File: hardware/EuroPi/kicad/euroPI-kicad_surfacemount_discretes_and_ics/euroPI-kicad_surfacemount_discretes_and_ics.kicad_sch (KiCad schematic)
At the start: 119 parts, among them J1 Output 1 Jack, J10 Eurorack Power 2x8 16p, J11 Conn_01x13_Socket, J12 OLED 64x128, J13 USB_B_Micro, J14 Conn_01x03_Pin, J15 Conn_01x04_Pin, J16 Conn_02x04_Top_Bottom, J17 Conn_01x13_Pin, J18 Conn_01x04_Pin, J19 Conn_01x04_Socket, J2 Output 2 Jack, J21 Conn_01x03_Pin, J3 Output 3 Jack, J4 Output 4 Jack, J5 Output 5 Jack, J6 Output 6 Jack, J7 Digital Input Jack, J8 Analogue Input Jack, Q1 2N2222, SW1 SW_Push, SW2 SW_Push, U3 LM555xN

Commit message: euroPI kicad version now including SMDs
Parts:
- C1, C10, C11, C12, C13, C14, C15, C16, C2, C3, C4, C5, C6, C7, C8, C9: footprint Capacitor_THT:C_Radial_D5.0mm_H11.0mm_P2.00mm -> Capacitor_SMD:C_0805_2012Metric_Pad1.18x1.45mm_HandSolder
- D1, D2, D3, D4: footprint Diode_THT:D_A-405_P2.54mm_Vertical_KathodeUp -> Diode_SMD:D_0805_2012Metric_Pad1.15x1.40mm_HandSolder
- O, O? (x8): footprint Package_DIP:DIP-14_W7.62mm_Socket -> Package_SO:SO-14_3.9x8.65mm_P1.27mm
- O1, O? (x2), U3: footprint Package_DIP:DIP-8_W7.62mm -> Package_SO:SO-8_3.9x4.9mm_P1.27mm
- Q1: footprint Package_TO_SOT_THT:TO-92 -> Package_TO_SOT_SMD:SOT-23
- R1, R10, R11, R12, R13, R14, R15, R16, R17, R18, R19, R2, R20, R21, R22, R23, R24, R25, R26, R27, R28, R29, R3, R30, R31, R32, R33, R34, R35, R36, R37, R38, R39, R4, R40, R5, R6, R7, R8, R9: footprint Resistor_THT:R_Axial_DIN0207_L6.3mm_D2.5mm_P5.08mm_Vertical -> Resistor_SMD:R_0805_2012Metric_Pad1.20x1.40mm_HandSolder
- U?: footprint Package_TO_SOT_THT:TO-220-3_Vertical -> Package_TO_SOT_SMD:TO-252-3_TabPin2

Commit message: kicad smd :)
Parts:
- D1, D2, D3, D4: footprint Diode_SMD:D_0805_2012Metric_Pad1.15x1.40mm_HandSolder -> Diode_SMD:D_SOD-123
- Q1: footprint Package_TO_SOT_SMD:SOT-23 -> Package_TO_SOT_THT:TO-92
- U?: footprint Package_TO_SOT_SMD:TO-252-3_TabPin2 -> Package_TO_SOT_THT:TO-220-3_Vertical
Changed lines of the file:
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@@
       (effects (font (size 1.27 1.27)))
     )
-    (property "Footprint" "Diode_SMD:D_0805_2012Metric_Pad1.15x1.40mm_HandSolder" (at 280.67 224.79 0)
+    (property "Footprint" "Diode_SMD:D_SOD-123" (at 280.67 224.79 0)
       (effects (font (size 1.27 1.27)) hide)
     )
@@
       (effects (font (size 1.27 1.27)) (justify left) hide)
     )
-    (property "Sim.Params" "type=\"D\" model=\"DIODE\" lib=\"\"" (at 191.77 5.08 0)
+    (property "Sim.Params" "1N4448W" (at 191.77 5.08 0)
       (effects (font (size 0 0)) hide)
     )
@@
       (effects (font (size 1.27 1.27)))
     )
-    (property "Footprint" "Diode_SMD:D_0805_2012Metric_Pad1.15x1.40mm_HandSolder" (at 364.49 186.69 0)
+    (property "Footprint" "Diode_SMD:D_SOD-123" (at 364.49 186.69 0)
       (effects (font (size 1.27 1.27)) hide)
     )
@@
       (effects (font (size 1.27 1.27)) (justify left) hide)
     )
-    (property "Sim.Params" "type=\"D\" model=\"DIODE\" lib=\"\"" (at 0 0 0)
+    (property "Sim.Params" "1N4448W" (at 0 0 0)
       (effects (font (size 0 0)) hide)
     )
@@
       (effects (font (size 1.27 1.27)) (justify left))
     )
-    (property "Footprint" "Package_TO_SOT_SMD:SOT-23" (at 374.65 177.165 0)
+    (property "Footprint" "Package_TO_SOT_THT:TO-92" (at 374.65 177.165 0)
       (effects (font (size 1.27 1.27) italic) (justify left) hide)
     )
@@
       (effects (font (size 1.27 1.27)))
     )
-    (property "Footprint" "Package_TO_SOT_SMD:TO-252-3_TabPin2" (at 52.705 87.63 0)
+    (property "Footprint" "Package_TO_SOT_THT:TO-220-3_Vertical" (at 52.705 87.63 0)
       (effects (font (size 1.27 1.27) italic) (justify left) hide)
     )
@@
       (effects (font (size 1.27 1.27)) hide)
     )
-    (property "Footprint" "Diode_SMD:D_0805_2012Metric_Pad1.15x1.40mm_HandSolder" (at 73.66 54.61 0)
+    (property "Footprint" "Diode_SMD:D_SOD-123" (at 73.66 54.61 0)
       (effects (font (size 1.27 1.27)) hide)
     )
@@
       (effects (font (size 1.27 1.27)) (justify left) hide)
     )
-    (property "Sim.Params" "type=\"D\" model=\"DIODE\" lib=\"\"" (at 3.81 7.62 0)
+    (property "Sim.Params" "1N4448W" (at 3.81 7.62 0)
       (effects (font (size 0 0)) hide)
     )
@@
       (effects (font (size 1.27 1.27)) hide)
     )
-    (property "Footprint" "Diode_SMD:D_0805_2012Metric_Pad1.15x1.40mm_HandSolder" (at 73.66 44.45 0)
+    (property "Footprint" "Diode_SMD:D_SOD-123" (at 73.66 44.45 0)
       (effects (font (size 1.27 1.27)) hide)
     )
@@
       (effects (font (size 1.27 1.27)) (justify left) hide)
     )
-    (property "Sim.Params" "type=\"D\" model=\"DIODE\" lib=\"\"" (at 3.81 7.62 0)
+    (property "Sim.Params" "1N4448W" (at 3.81 7.62 0)
       (effects (font (size 0 0)) hide)
     )

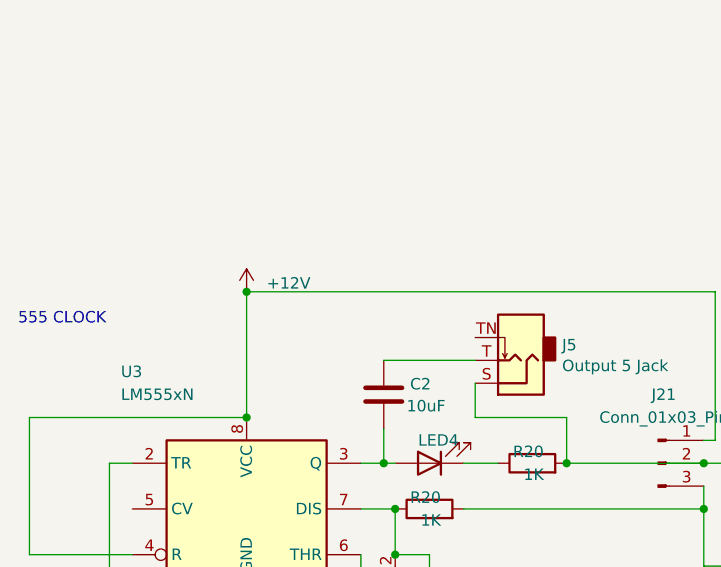
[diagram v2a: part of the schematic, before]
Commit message: misc improvements THT fixed grounds and misc clean up issue likely still wtih usb output SMT redid caps to be near to necessary fixed GND and misc things to make it easier to hand solder
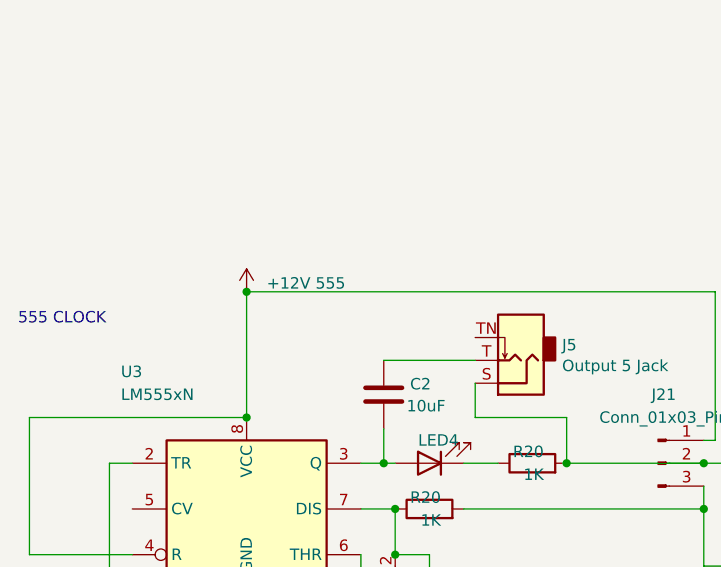
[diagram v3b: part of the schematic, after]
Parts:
- Reference?: value +12V -> +12V 555
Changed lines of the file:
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@@
       (effects (font (size 1.27 1.27)) hide)
     )
-    (property "Value" "+12V" (at -93.0148 85.4202 0)
+    (property "Value" "+12V 555" (at -93.0148 85.4202 0)
       (effects (font (size 1.27 1.27)) (justify left))
     )

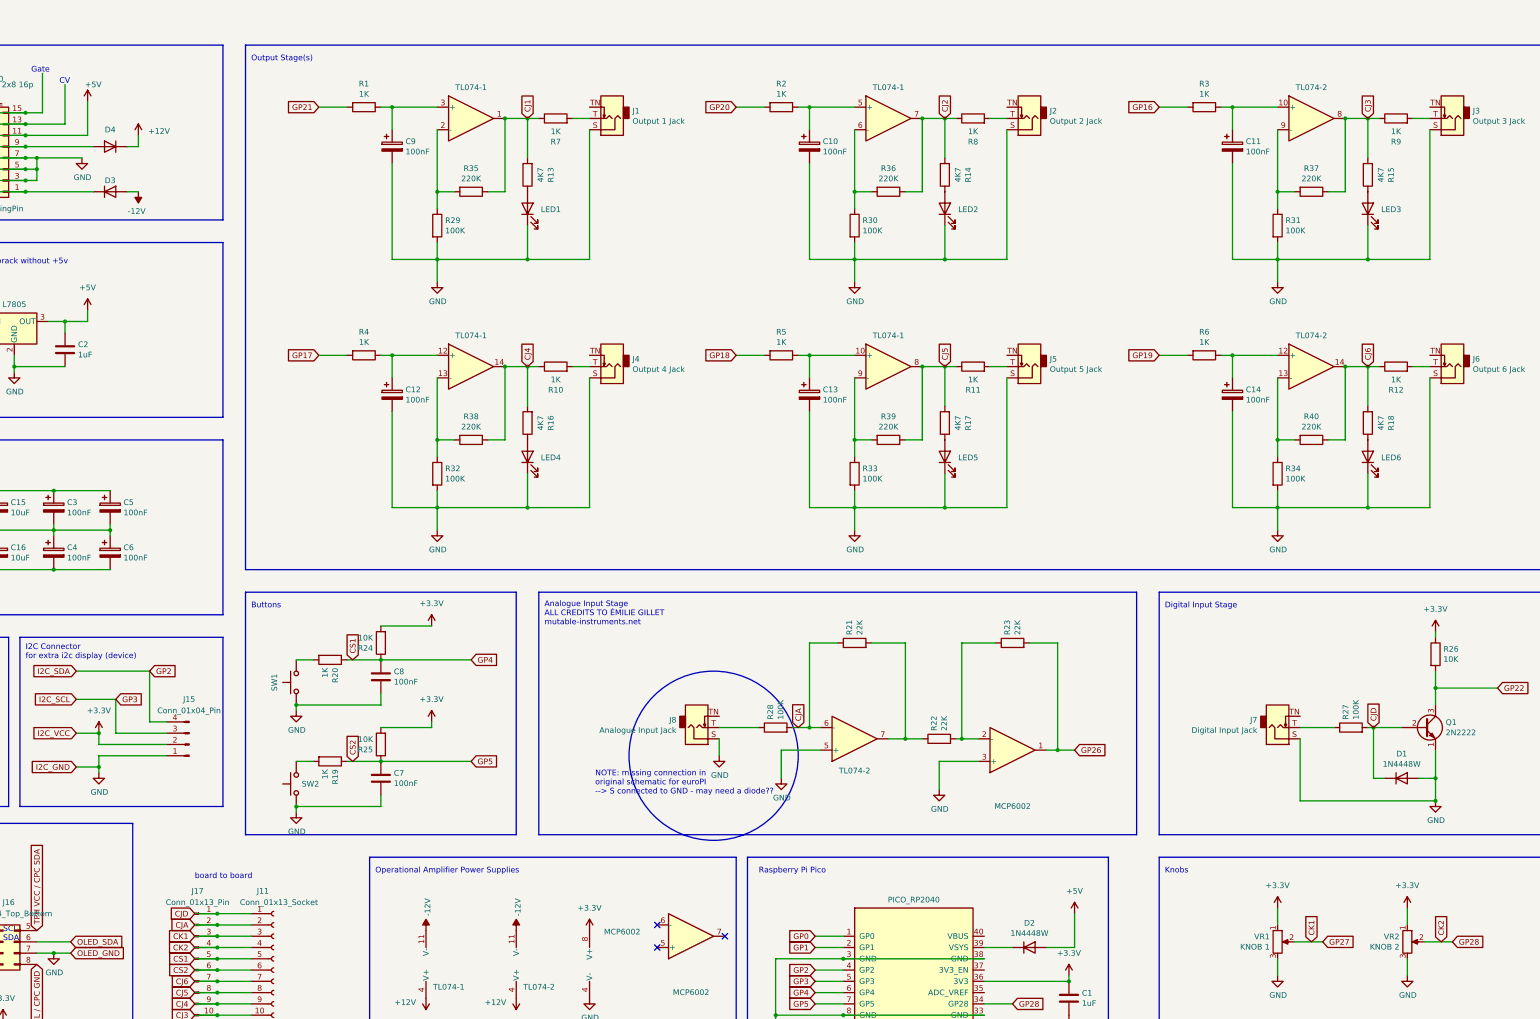
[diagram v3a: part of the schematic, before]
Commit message: some updates of smt version incl correcting layout component choices support structures
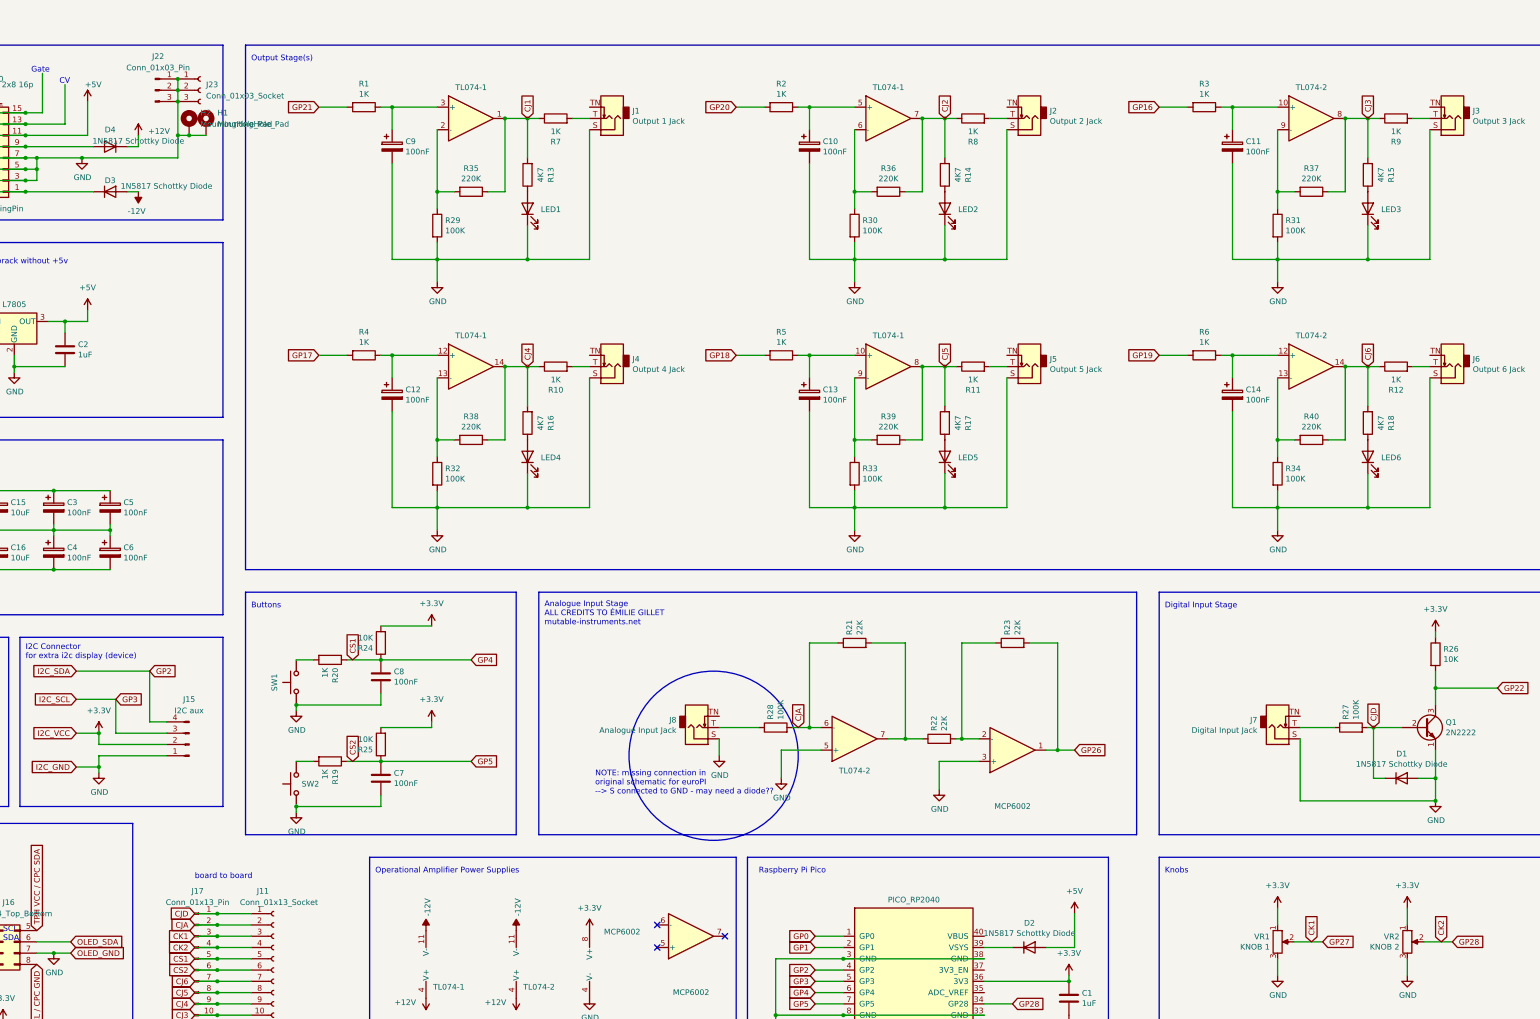
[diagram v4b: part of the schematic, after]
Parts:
- added H1, H2: MountingHole_Pad, MountingHole:MountingHole_2.5mm_Pad_TopOnly, symbol Mechanical:MountingHole_Pad
- added J22: Conn_01x03_Pin, Connector_PinHeader_2.54mm:PinHeader_1x03_P2.54mm_Vertical, symbol Connector:Conn_01x03_Pin
- added J23: Conn_01x03_Socket, Connector_PinSocket_2.54mm:PinSocket_1x03_P2.54mm_Vertical, symbol Connector:Conn_01x03_Socket
- C15, C16, C3, C4, C5, C6: footprint Capacitor_SMD:C_0805_2012Metric_Pad1.18x1.45mm_HandSolder -> Library:CP_Radial_D5.0mm_P2.50mm
- D1, D2, D3, D4: value ${SIM.PARAMS} -> 1N5817 Schottky Diode; footprint Diode_SMD:D_SOD-123 -> Diode_THT:D_DO-41_SOD81_P7.62mm_Horizontal
- J15: value Conn_01x04_Pin -> I2C aux
- Q1: footprint Package_TO_SOT_THT:TO-92 -> Package_TO_SOT_THT:TO-92_Inline_Wide
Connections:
- net GND: now also H1.1, H2.1, J22.1 (Pin_1), J22.2 (Pin_2), J22.3 (Pin_3), J23.1 (Pin_1), J23.2 (Pin_2), J23.3 (Pin_3)
